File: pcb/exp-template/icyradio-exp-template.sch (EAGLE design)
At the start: 3 parts

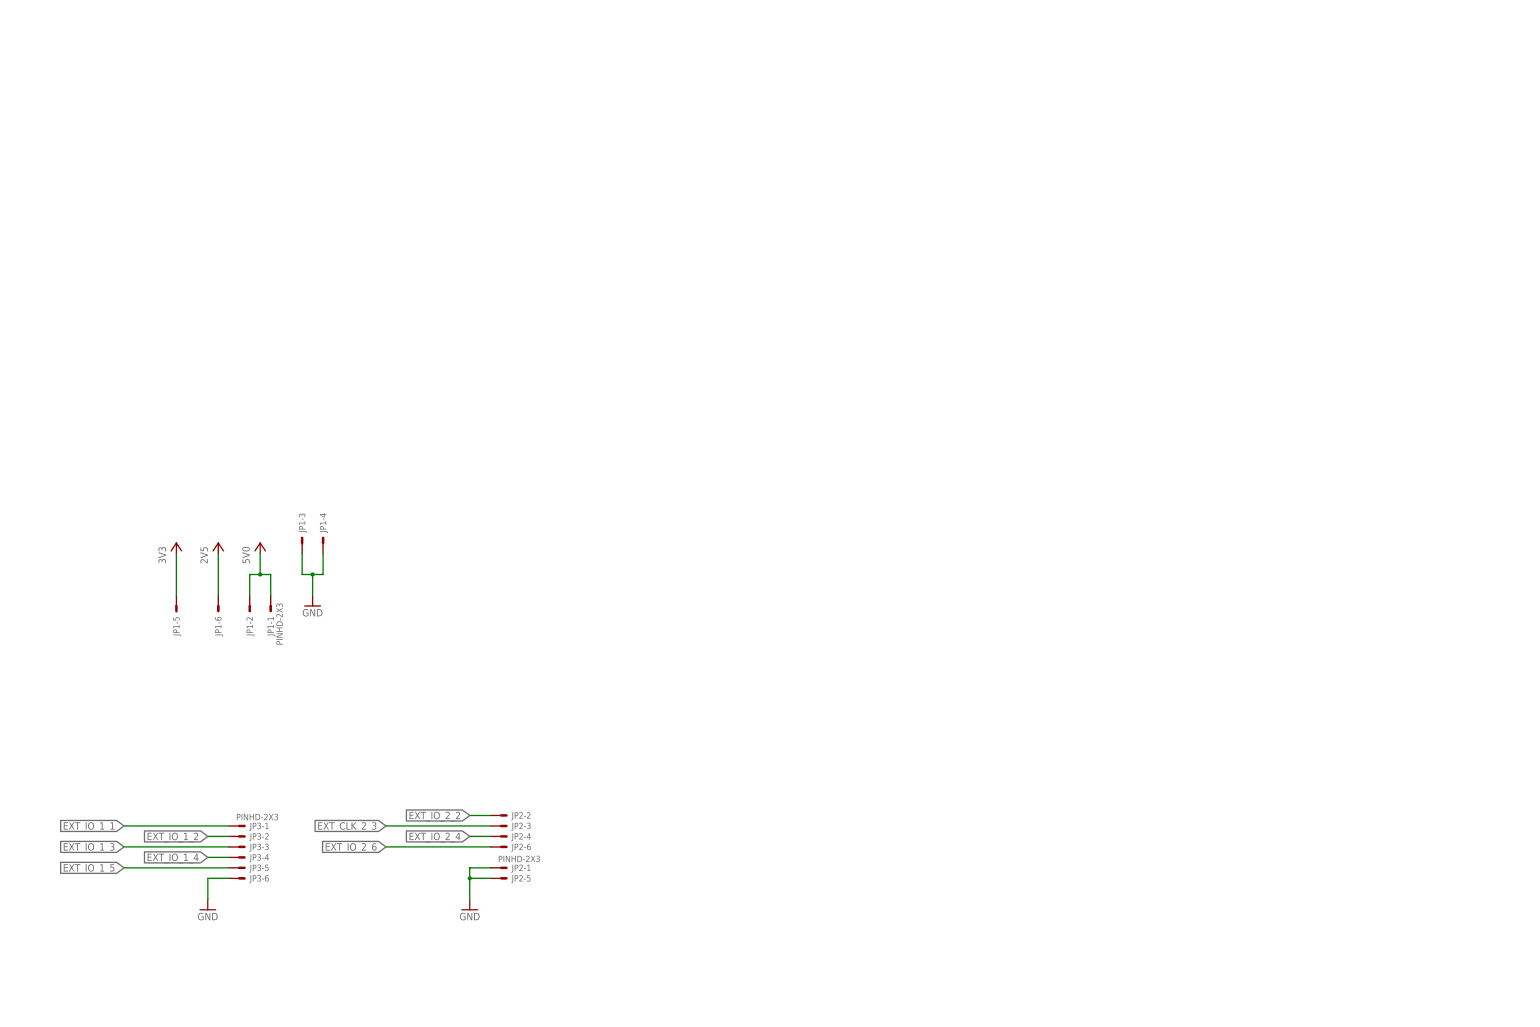
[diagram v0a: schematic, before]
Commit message: Add expansion board PCB template
Signed-off-by: João Silva <jgc3silva@gmail.com>
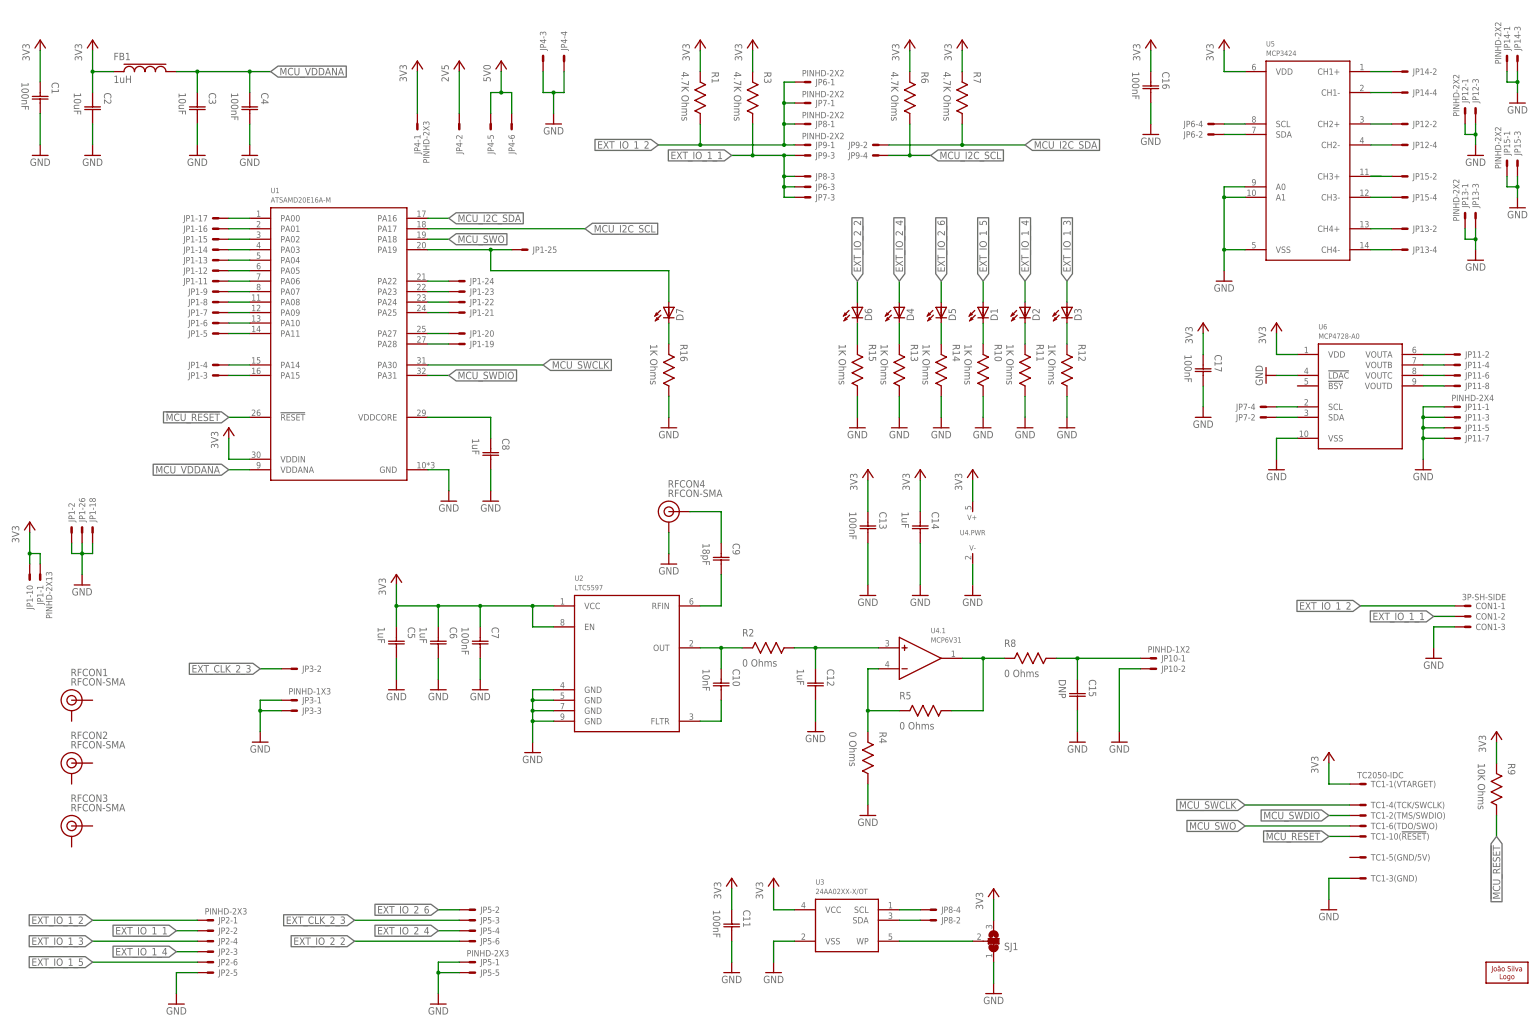
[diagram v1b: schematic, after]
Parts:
- added C1, C11, C13, C16, C17, C4, C7: 100nF, Capacitor:CAPACITOR-0402
- added C10: 10nF, Capacitor:CAPACITOR-0402
- added C12, C14, C5, C6, C8: 1uF, Capacitor:CAPACITOR-0402
- added C15: DNP, Capacitor:CAPACITOR-0402
- added C2, C3: 10uF, Capacitor:CAPACITOR-0402
- added C9: 18pF, Capacitor:CAPACITOR-0402
- added CON1: 3P-SH-SIDE, JST:3P-SH-SIDE
- added D1, D2, D3, D4, D5, D6, D7: LED0603, LED:LED0603
- added FB1: 1uH, Inductor:FERRITE-0603
- added JP10: PINHD-1X2, Pin Header:PINHD-1X2
- added JP11: PINHD-2X4, Pin Header:PINHD-2X4
- added JP12, JP13, JP14, JP15, JP6, JP7, JP8, JP9: PINHD-2X2, Pin Header:PINHD-2X2
- added JP4, JP5: PINHD-2X3, Pin Header:PINHD-2X3
- added LOGO1: JSILVA-5MM, Silkscreen:JSILVA-5MM
- added R1, R3, R6, R7: 4.7K Ohms, Resistor:RESISTOR-0402
- added R10, R11, R12, R13, R14, R15, R16: 1K Ohms, Resistor:RESISTOR-0402
- added R2, R4, R5, R8: 0 Ohms, Resistor:RESISTOR-0402
- added R9: 10K Ohms, Resistor:RESISTOR-0402
- added RFCON1, RFCON2, RFCON3, RFCON4: RFCON-SMA, RF Connector:RFCON-SMA
- added SJ1: (no value), Solder Jumper:SJ2CS
- added TC1: TC2050-IDC, TagConnect:TC2050-IDC
- added U1: ATSAMD20E16A-M, Microchip:ATSAMD20E16A-M
- added U2: LTC5597, Analog Devices:LTC5597
- added U3: 24AA02XX-X/OT, Microchip:24AA02XX-X/OT
- added U4: MCP6V31, Microchip:MCP6V31
- added U5: MCP3424, Microchip:MCP3424
- added U6: MCP4728-A0, Microchip:MCP4728-A0
- JP1: value PINHD-2X3 -> PINHD-2X13; device Pin Header:PINHD-2X3 -> Pin Header:PINHD-2X13
- JP3: value PINHD-2X3 -> PINHD-1X3; device Pin Header:PINHD-2X3 -> Pin Header:PINHD-1X3
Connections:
- new net !MCU_RESET: R9.1, TC1-10(!RESET!).S, U1.!RESET
- new net ADC_C1_N: JP14-4.S, U5.CH1-
- new net ADC_C1_P: JP14-2.S, U5.CH1+
- new net ADC_C2_N: JP12-4.S, U5.CH2-
- new net ADC_C2_P: JP12-2.S, U5.CH2+
- new net ADC_C3_N: JP15-4.S, U5.CH3-
- new net ADC_C3_P: JP15-2.S, U5.CH3+
- new net ADC_C4_N: JP13-4.S, U5.CH4-
- new net ADC_C4_P: JP13-2.S, U5.CH4+
- new net ADC_I2C_SCL: JP6-4.S, U5.SCL
- new net ADC_I2C_SDA: JP6-2.S, U5.SDA
- new net DAC_I2C_SCL: JP7-4.S, U6.SCL
- new net DAC_I2C_SDA: JP7-2.S, U6.SDA
- new net DAC_VA: JP11-2.S, U6.VOUTA
- new net DAC_VB: JP11-4.S, U6.VOUTB
- new net DAC_VC: JP11-6.S, U6.VOUTC
- new net DAC_VD: JP11-8.S, U6.VOUTD
- new net EE_I2C_SCL: JP8-4.S, U3.SCL
- new net EE_I2C_SDA: JP8-2.S, U3.SDA
- new net EE_WP: SJ1.2, U3.WP
- new net MCU_I2C_SCL: JP9-4.S, R6.1, U1.PA17
- new net MCU_I2C_SDA: JP9-2.S, R7.1, U1.PA16
- new net MCU_SWCLK: TC1-4(TCK/SWCLK).S, U1.PA30
- new net MCU_SWDIO: TC1-2(TMS/SWDIO).S, U1.PA31
- new net MCU_SWO: TC1-6(TDO/SWO).S, U1.PA18
- new net MCU_VDDANA: C3.C1, C4.C1, FB1.2, U1.VDDANA
- new net N$1: C8.C1, U1.VDDCORE
- new net N$14: R5.1, R8.2, U4.1.OUT
- new net N$15: C10.C2, U2.FLTR
- new net N$16: C10.C1, R2.2, U2.OUT
- new net N$17: C12.C1, R2.1, U4.1.+IN
- new net N$18: R4.2, R5.2, U4.1.-IN
- new net N$19: C9.C1, RFCON4.SIGNAL
- new net N$2: D1.C, R10.2
- new net N$20: C9.C2, U2.RFIN
- new net N$21: C15.C1, JP10-1.S, R8.1
- new net N$3: D2.C, R11.2
- new net N$4: D3.C, R12.2
- new net N$5: D4.C, R13.2
- new net N$6: D5.C, R14.2
- new net N$7: D6.C, R15.2
- new net N$8: D7.C, R16.2
- new net P0: JP1-17.S, U1.PA00
- new net P1: JP1-16.S, U1.PA01
- new net P10: JP1-6.S, U1.PA10
- new net P11: JP1-5.S, U1.PA11
- new net P14: JP1-4.S, U1.PA14
- new net P15: JP1-3.S, U1.PA15
- new net P19: D7.A, JP1-25.S, U1.PA19
- new net P2: JP1-15.S, U1.PA02
- new net P22: JP1-24.S, U1.PA22
- new net P23: JP1-23.S, U1.PA23
- new net P24: JP1-22.S, U1.PA24
- new net P25: JP1-21.S, U1.PA25
- new net P27: JP1-20.S, U1.PA27
- new net P28: JP1-19.S, U1.PA28
- new net P3: JP1-14.S, U1.PA03
- new net P4: JP1-13.S, U1.PA04
- new net P5: JP1-12.S, U1.PA05
- new net P6: JP1-11.S, U1.PA06
- new net P7: JP1-9.S, U1.PA07
- new net P8: JP1-8.S, U1.PA08
- new net P9: JP1-7.S, U1.PA09
- net 2V5: now also JP4-2.S; no longer JP1-6.S
- net 3V3: now also C1.C1, C11.C1, C13.C1, C14.C1, C16.C1, C17.C1, C2.C1, C5.C1, C6.C1, C7.C1, FB1.1, JP1-1.S, JP1-10.S, JP4-1.S, R1.2, R3.2, R6.2, R7.2, R9.2, SJ1.3, TC1-1(VTARGET).S, U1.VDDIN, U2.EN, U2.VCC, U3.VCC, U4.PWR.V+, U5.VDD, U6.VDD; no longer JP1-5.S
- net 5V0: now also JP4-5.S, JP4-6.S; no longer JP1-1.S, JP1-2.S
- net EXT_CLK_2_3: now also JP3-2.S, JP5-3.S; no longer JP2-3.S
- net EXT_IO_1_1: now also CON1-2.S, JP2-2.S, JP6-3.S, JP7-3.S, JP8-3.S, JP9-3.S, R3.1; no longer JP3-1.S
- net EXT_IO_1_2: now also CON1-1.S, JP2-1.S, JP6-1.S, JP7-1.S, JP8-1.S, JP9-1.S, R1.1; no longer JP3-2.S
- net EXT_IO_1_3: now also D3.A, JP2-4.S; no longer JP3-3.S
- net EXT_IO_1_4: now also D2.A, JP2-3.S; no longer JP3-4.S
- net EXT_IO_1_5: now also D1.A, JP2-6.S; no longer JP3-5.S
- net EXT_IO_2_2: now also D6.A, JP5-6.S; no longer JP2-2.S
- net EXT_IO_2_4: now also D4.A, JP5-4.S; no longer JP2-4.S
- net EXT_IO_2_6: now also D5.A, JP5-2.S; no longer JP2-6.S
- net GND: now also C1.C2, C11.C2, C12.C2, C13.C2, C14.C2, C15.C2, C16.C2, C17.C2, C2.C2, C3.C2, C4.C2, C5.C2, C6.C2, C7.C2, C8.C2, CON1-3.S, JP1-18.S, JP1-2.S, JP1-26.S, JP10-2.S, JP11-1.S, JP11-3.S, JP11-5.S, JP11-7.S, JP12-1.S, JP12-3.S, JP13-1.S, JP13-3.S, JP14-1.S, JP14-3.S, JP15-1.S, JP15-3.S, JP3-1.S, JP3-3.S, JP4-3.S, JP4-4.S, JP5-1.S, JP5-5.S, R10.1, R11.1, R12.1, R13.1, R14.1, R15.1, R16.1, R4.1, RFCON4.GND, SJ1.1, TC1-3(GND).S, U1.GND, U2.GND@0, U2.GND@1, U2.GND@2, U2.GND@3, U3.VSS, U4.PWR.V-, U5.A0, U5.A1, U5.VSS, U6.!LDAC, U6.VSS; no longer JP1-3.S, JP1-4.S, JP2-1.S, JP3-6.S
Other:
- moved on the sheet: JP1-1, JP1-2, JP1-3, JP1-4, JP1-5, JP1-6, JP2-1, JP2-2, JP2-3, JP2-4, JP2-5, JP2-6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
